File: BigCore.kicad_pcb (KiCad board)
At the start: 4 copper layers, 61 x 100 mm, 151 parts, among them J1 5V In, J10 Btn 3, J11 GND, J12 USB_C_Receptacle_USB2.0, J13 Line Out, J14 Servo 01, J15 Servo 02, J16 Servo 03, J17 Servo 04, J18 Servo 05, J19 Servo 06, J2 Vdrive In, J20 I2C, J22 WS2812, J3 JTAG, J4 DM3AT-SF-PEJM5, J5 Volume, J6 Btn 0, J7 RS485, J8 Btn 1, J9 Btn 2, Q1 SS8050-G, Q2 SS8050-G, SW1 Reset, SW2 Boot, SW3 Btn 0, SW4 Btn 1, SW5 Btn 2, SW6 Btn 3, U1 AP63203WU, U10 74AHCT1G17, U2 AP2112K-3.3, U3 ESP32-WROOM-32E, U4 ST3485EBDR, U5 USBLC6-2SC6, U6 CP2102N-Axx-xQFN24, U7 PCM5102A, U9 74AHCT1G17

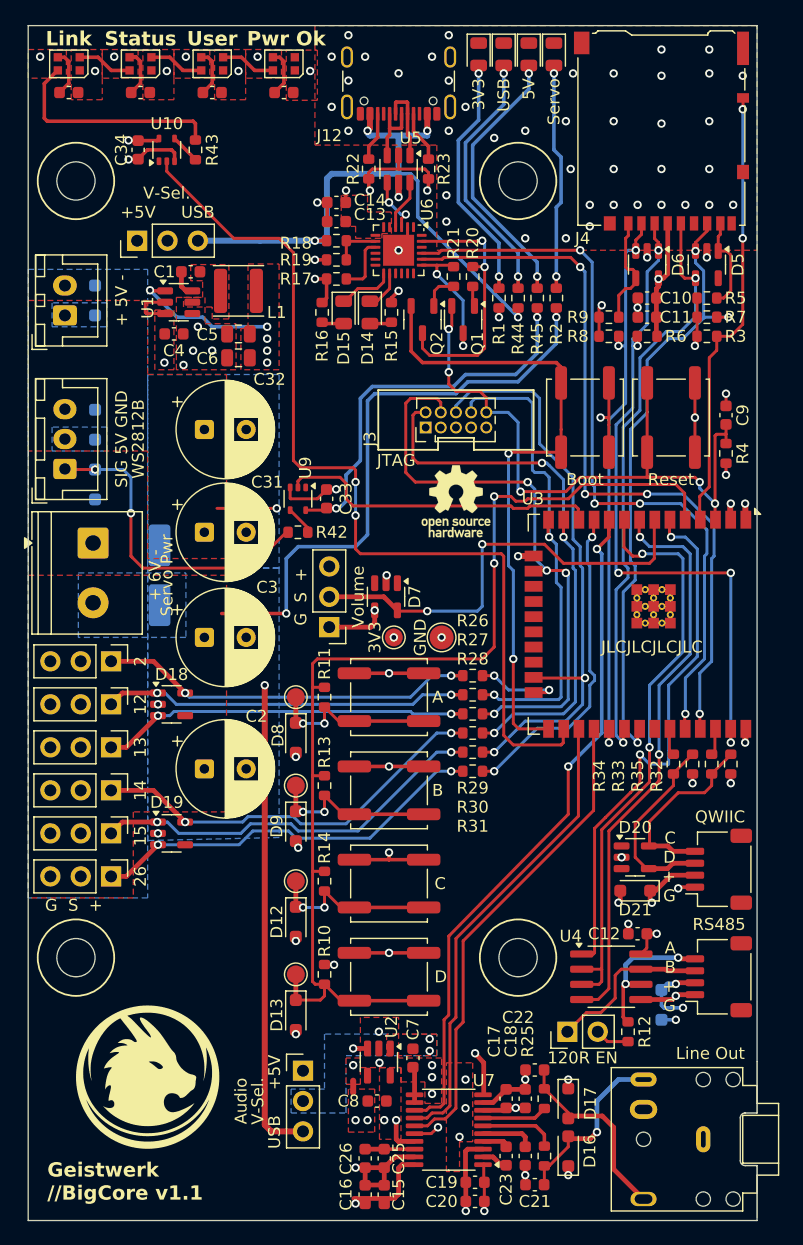
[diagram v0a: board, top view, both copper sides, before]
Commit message: Changed some labes, fixed RS485 Line Fixed Servo-Pin Header and Audio-Pin Header label. Added 10k Pullup to RS485 R-Line
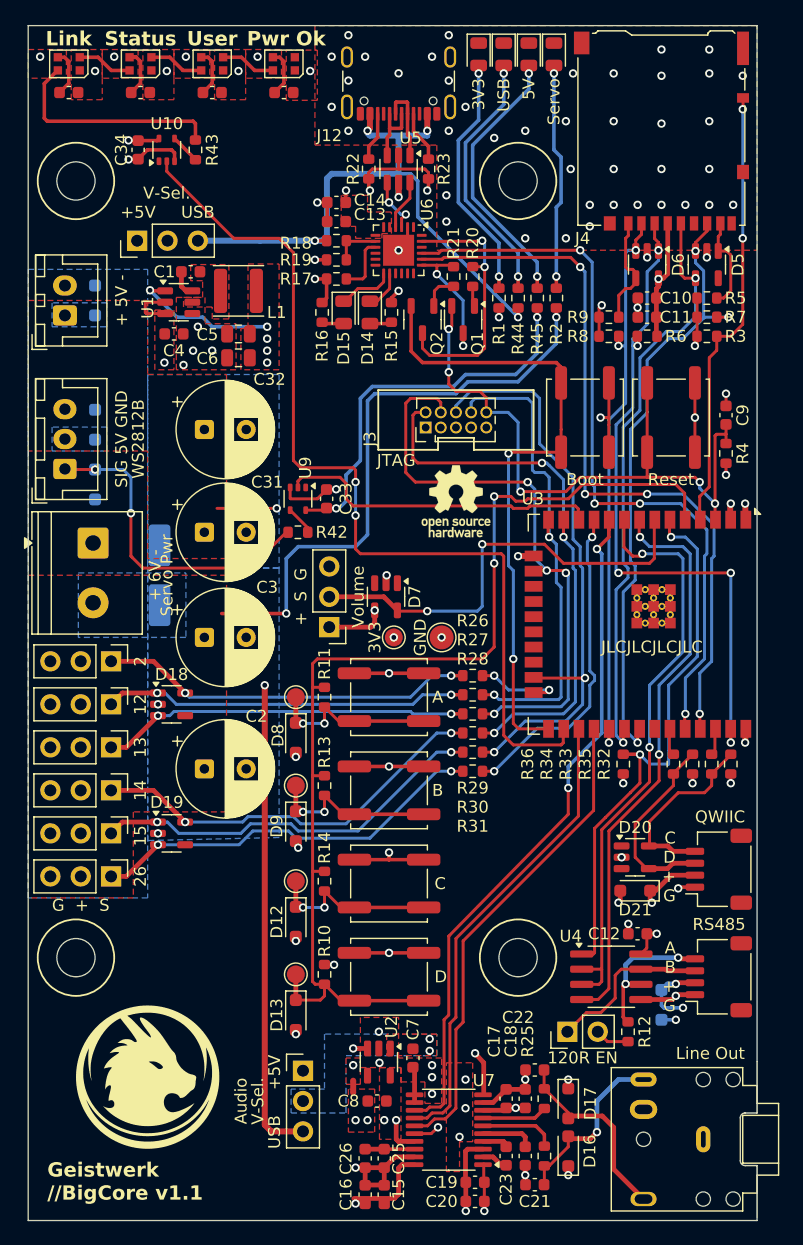
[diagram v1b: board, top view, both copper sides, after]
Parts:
- added R36: 10k, Resistor_SMD:R_0603_1608Metric, F.Cu at (132.8, 163.8)
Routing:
- net /Controller/RS485_R: track 45.1 -> 46.5 mm
- net +3.3V: track 66.7 -> 67.5 mm, vias 24 -> 25
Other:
- board text added: "+ S G"
- board text added: "G + S"
- board text removed: "G S +"
